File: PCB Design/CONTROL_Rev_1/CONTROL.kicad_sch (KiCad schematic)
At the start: 4 parts, among them J1 Conn_01x24_Pin, J2 Conn_01x24_Pin, U1 STM32F446RETx

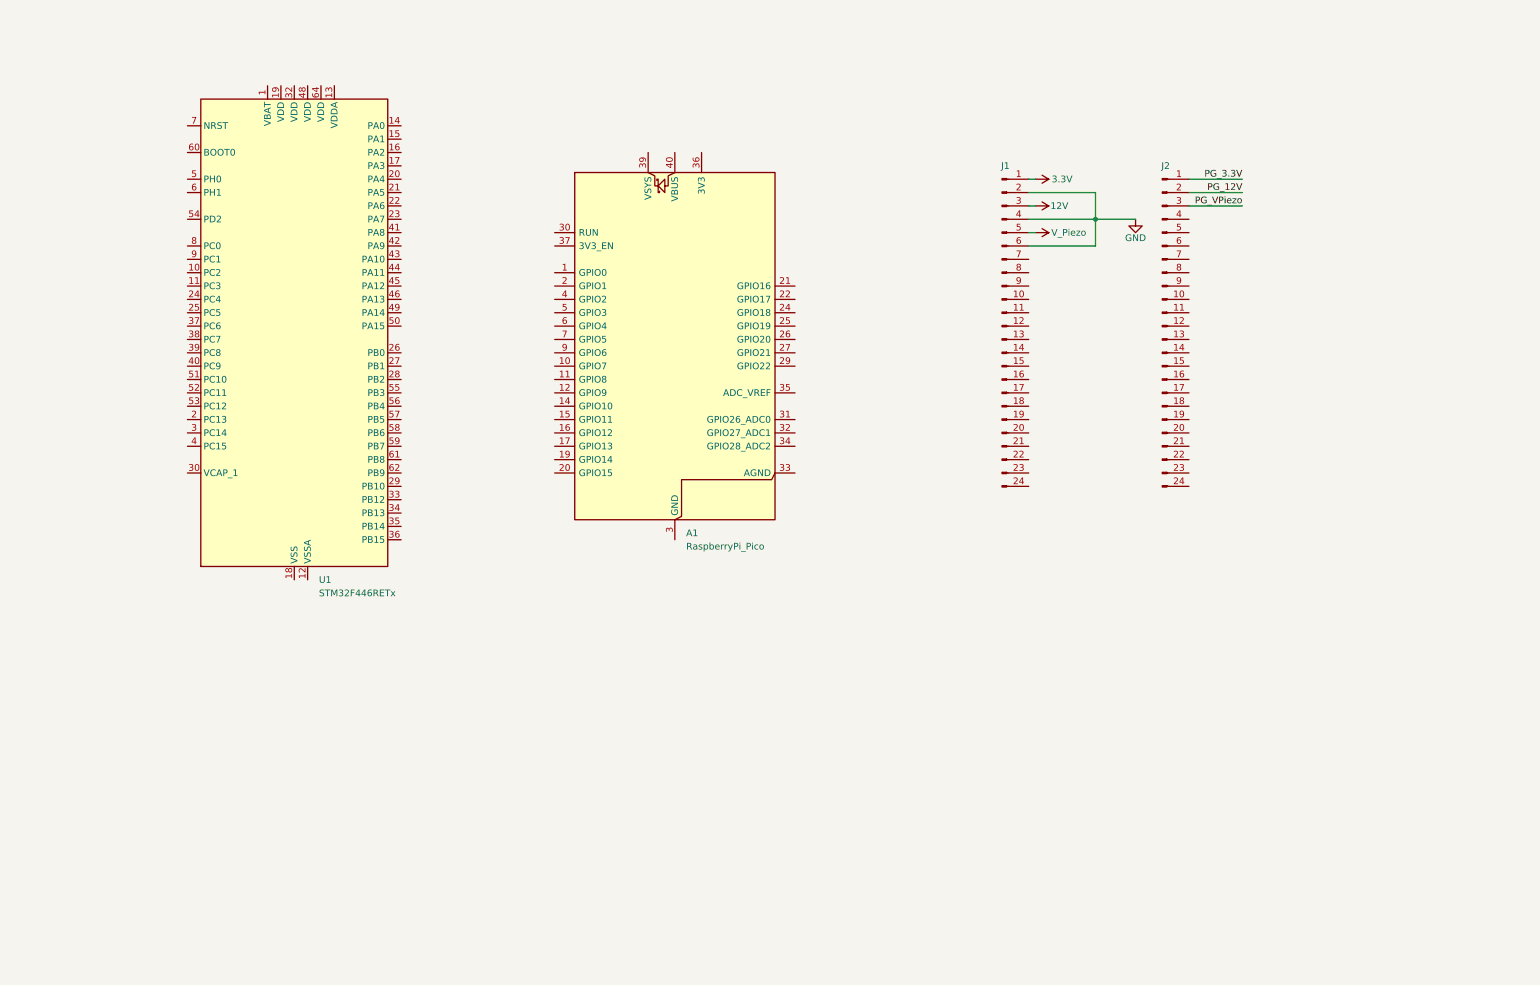
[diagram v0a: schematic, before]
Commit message: Initial Component Layout of Main MCU
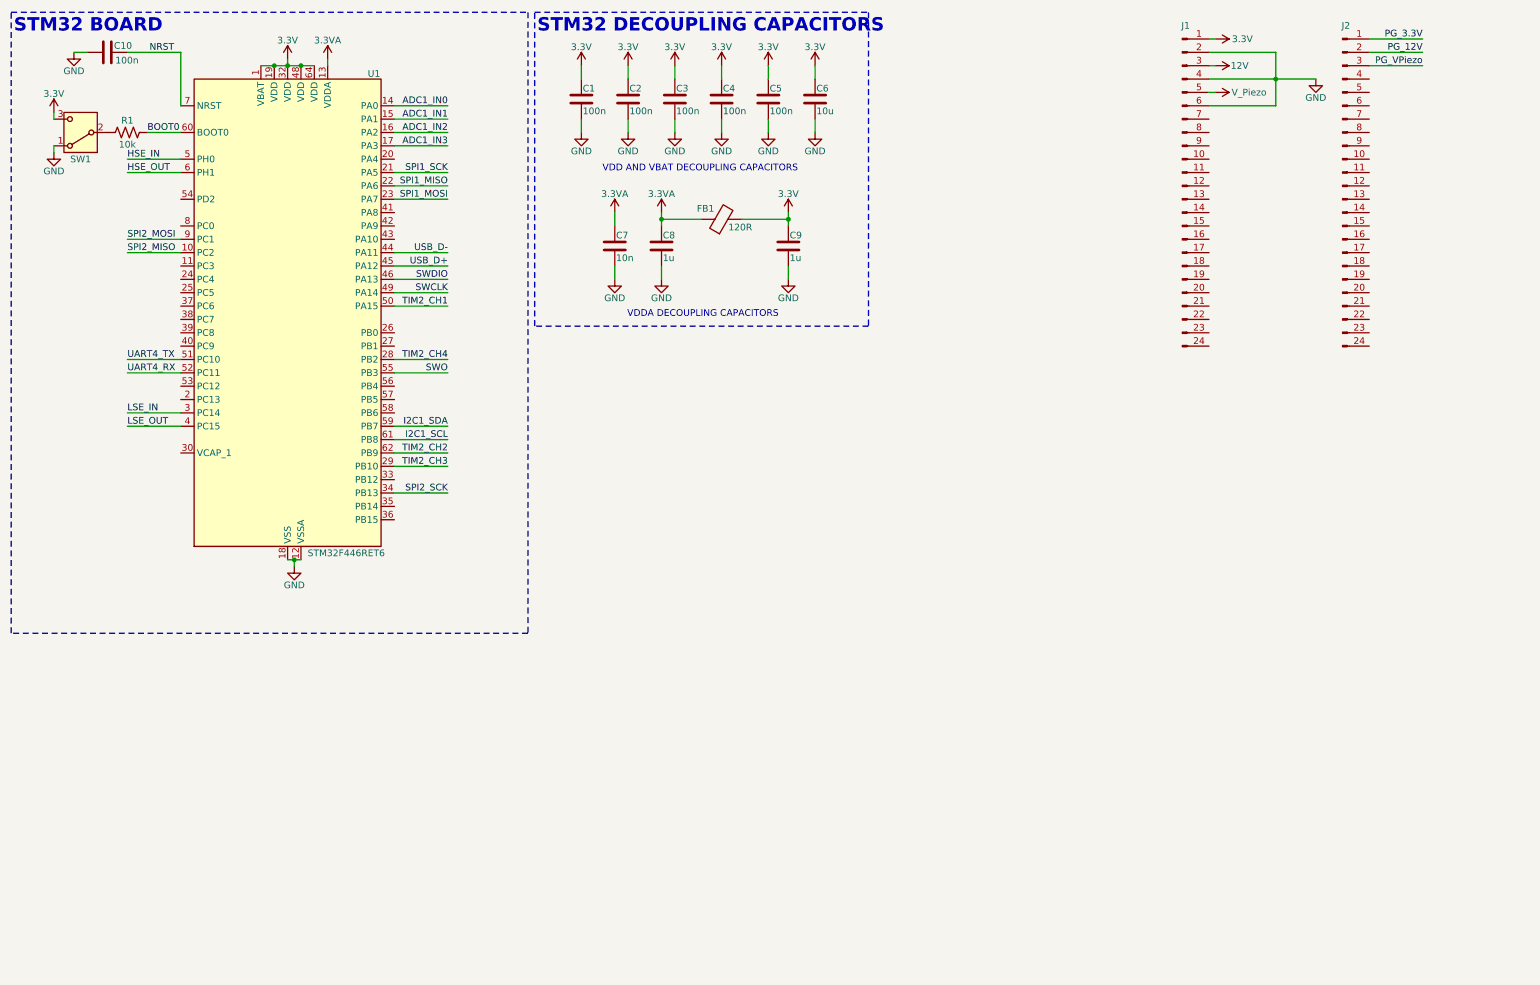
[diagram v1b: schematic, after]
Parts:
- removed A1: RaspberryPi_Pico, Module:RaspberryPi_Pico_Common_Unspecified, symbol MCU_Module:RaspberryPi_Pico
- added C1, C10, C2, C3, C4, C5: 100n, Capacitor_SMD:C_0603_1608Metric, symbol Device:C
- added C6: 10u, Capacitor_SMD:C_0603_1608Metric, symbol Device:C
- added C7: 10n, Capacitor_SMD:C_0603_1608Metric, symbol Device:C
- added C8, C9: 1u, Capacitor_SMD:C_0603_1608Metric, symbol Device:C
- added FB1: 120R, symbol Device:FerriteBead
- added R1: 10k, symbol Device:R_US
- added SW1: SW_SPDT, symbol Switch:SW_SPDT
- U1: value STM32F446RETx -> STM32F446RET6
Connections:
- net 3.3V: now also U1.1 (VBAT), U1.19 (VDD), U1.32 (VDD), U1.48 (VDD), U1.64 (VDD), C1.1, C2.1, C3.1, C4.1, C5.1, C6.1, C9.1, FB1.2, SW1.3 (C)
- net GND: now also U1.12 (VSSA), U1.18 (VSS), U1.31 (VSS), U1.47 (VSS), U1.63 (VSS), C1.2, C10.1, C2.2, C3.2, C4.2, C5.2, C6.2, C7.2, C8.2, C9.2, SW1.1 (A)
- net SPI2_MISO: now reaches U1.10 (PC2)
- net 3.3VA: now reaches U1.13 (VDDA)
- net 3.3VA: now also C7.1, C8.1, FB1.1
- net ADC1_IN0: now reaches U1.14 (PA0)
- net ADC1_IN1: now reaches U1.15 (PA1)
- net ADC1_IN2: now reaches U1.16 (PA2)
- net ADC1_IN3: now reaches U1.17 (PA3)
- net SPI1_SCK: now reaches U1.21 (PA5)
- net SPI1_MISO: now reaches U1.22 (PA6)
- net SPI1_MOSI: now reaches U1.23 (PA7)
- net TIM2_CH4: now reaches U1.28 (PB2)
- net TIM2_CH3: now reaches U1.29 (PB10)
- net LSE_IN: now reaches U1.3 (PC14)
- net SPI2_SCK: now reaches U1.34 (PB13)
- net LSE_OUT: now reaches U1.4 (PC15)
- net USB_D-: now reaches U1.44 (PA11)
- net USB_D+: now reaches U1.45 (PA12)
- net SWDIO: now reaches U1.46 (PA13)
- net SWCLK: now reaches U1.49 (PA14)
- net HSE_IN: now reaches U1.5 (PH0)
- net TIM2_CH1: now reaches U1.50 (PA15)
- net UART4_TX: now reaches U1.51 (PC10)
- net UART4_RX: now reaches U1.52 (PC11)
- net SWO: now reaches U1.55 (PB3)
- net I2C1_SDA: now reaches U1.59 (PB7)
- net HSE_OUT: now reaches U1.6 (PH1)
- net BOOT0: now reaches U1.60 (BOOT0)
- net BOOT0: now also R1.2
- net I2C1_SCL: now reaches U1.61 (PB8)
- net TIM2_CH2: now reaches U1.62 (PB9)
- net NRST: now reaches U1.7 (NRST)
- net NRST: now also C10.2
- net SPI2_MOSI: now reaches U1.9 (PC1)
- new net: R1.1, SW1.2 (B)
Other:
- note added: "STM32 BOARD"
- note added: "STM32 DECOUPLING CAPACITORS"
- note added: "VDD AND VBAT DECOUPLING CAPACITORS"
- note added: "VDDA DECOUPLING CAPACITORS"
- moved on the sheet: J1, J2, U1

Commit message: Finished Schematic, Started Placing Components on PCB
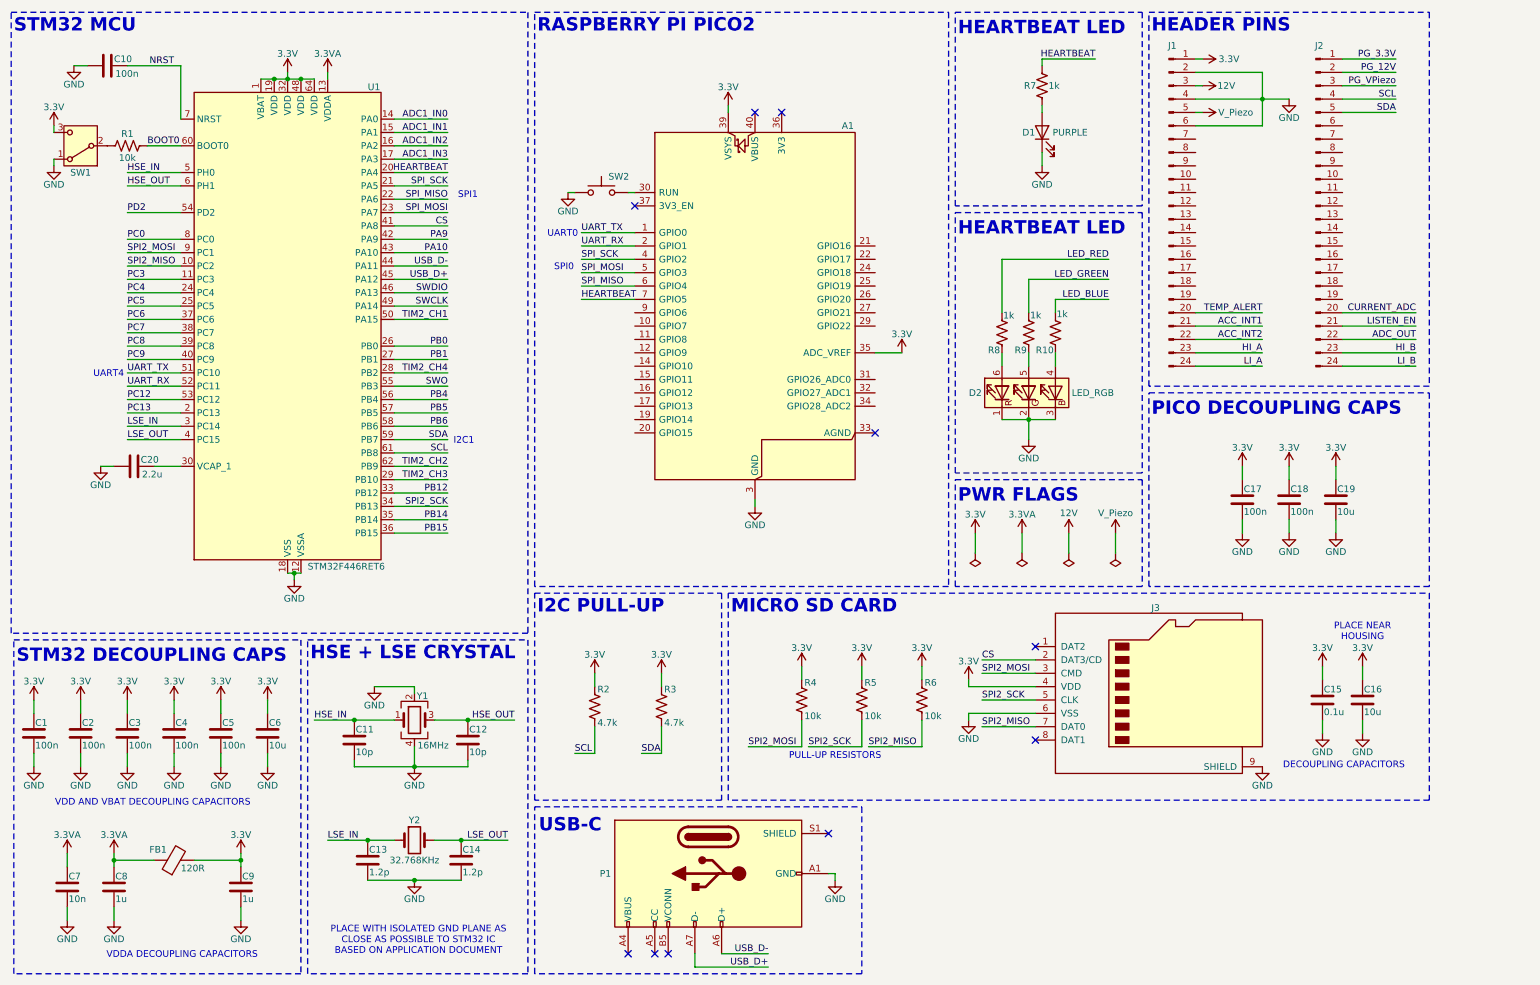
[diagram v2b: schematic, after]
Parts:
- added A1: RaspberryPi_Pico, Module:RaspberryPi_Pico_Common_Unspecified, symbol MCU_Module:RaspberryPi_Pico
- added C11, C12: 10p, Capacitor_SMD:C_0603_1608Metric, symbol Device:C
- added C13, C14: 1.2p, Capacitor_SMD:C_0603_1608Metric, symbol Device:C
- added C15: 0.1u, Capacitor_SMD:C_0603_1608Metric, symbol Device:C
- added C16, C19: 10u, Capacitor_SMD:C_0603_1608Metric, symbol Device:C
- added C17, C18: 100n, Capacitor_SMD:C_0603_1608Metric, symbol Device:C
- added C20: 2.2u, Capacitor_SMD:C_0603_1608Metric, symbol Device:C
- added D1: PURPLE, CONTROL:JB2835AWTWU57EA0000N0000001, symbol Device:LED
- added D2: LED_RGB, LED_SMD:LED_RGB_PLCC-6, symbol Device:LED_RGB
- added J3: Micro_SD_Card, CONTROL:AMPHENOL_1140084168, symbol Connector:Micro_SD_Card
- added P1: USB_C_Plug_USB2.0, CONTROL:AMPHENOL_10164359-00011LF, symbol Connector:USB_C_Plug_USB2.0
- added R10, R7, R8, R9: 1k, Resistor_SMD:R_0603_1608Metric, symbol Device:R_US
- added R2, R3: 4.7k, Resistor_SMD:R_0603_1608Metric, symbol Device:R_US
- added R4, R5, R6: 10k, Resistor_SMD:R_0603_1608Metric, symbol Device:R_US
- added SW2: SW_Push, Button_Switch_SMD:SW_Tactile_SPST_NO_Straight_CK_PTS636Sx25SMTRLFS, symbol Switch:SW_Push
- added Y1: 16MHz, symbol Device:Crystal_GND24
- added Y2: 32.768KHz, CONTROL:XTAL_ABS05W-32.768KHZ-D-2-T, symbol Device:Crystal
- FB1: footprint (none) -> Inductor_SMD:L_0201_0603Metric
- R1: footprint (none) -> Resistor_SMD:R_0603_1608Metric
- SW1: footprint (none) -> CONTROL:B-TYPE
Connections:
- net I2C1_SCL is gone; now on net SCL: U1.61 (PB8)
- net I2C1_SDA is gone; now on net SDA: U1.59 (PB7)
- net 3.3V: now also A1.35 (ADC_VREF), A1.39 (VSYS), C15.1, C16.1, C17.1, C18.1, C19.1, J3.4 (VDD), R2.1, R3.1, R4.1, R5.1, R6.1
- net GND: now also A1.13 (GND), A1.18 (GND), A1.23 (GND), A1.28 (GND), A1.3 (GND), A1.38 (GND), A1.8 (GND), C11.2, C12.2, C13.2, C14.2, C15.2, C16.2, C17.2, C18.2, C19.2, C20.1, D1.1 (K), D2.1 (RK), D2.2 (GK), D2.3 (BK), J3.6 (VSS), J3.9 (SHIELD), P1.A1 (GND), P1.A12 (GND), P1.B1 (GND), P1.B12 (GND), SW2.1, Y1.2, Y1.4
- net HSE_IN: now also C11.1, Y1.1
- net HSE_OUT: now also C12.1, Y1.3
- net LSE_IN: now also C13.1, Y2.1
- net LSE_OUT: now also C14.1, Y2.2
- net SPI2_MISO: now also J3.7 (DAT0), R6.2
- net SPI2_MOSI: now also J3.3 (CMD), R4.2
- net SPI2_SCK: now also J3.5 (CLK), R5.2
- net USB_D+: now also P1.A7 (D-)
- net USB_D-: now also P1.A6 (D+)
- net CURRENT_ADC: now reaches J2.20 (Pin_20)
- net LISTEN_EN: now reaches J2.21 (Pin_21)
- net ADC_OUT: now reaches J2.22 (Pin_22)
- net HI_B: now reaches J2.23 (Pin_23)
- net LI_B: now reaches J2.24 (Pin_24)
- net SCL: now reaches J2.4 (Pin_4)
- net SCL: now also R2.2
- net SDA: now reaches J2.5 (Pin_5)
- net SDA: now also R3.2
- net TEMP_ALERT: now reaches J1.20 (Pin_20)
- net ACC_INT1: now reaches J1.21 (Pin_21)
- net ACC_INT2: now reaches J1.22 (Pin_22)
- net HI_A: now reaches J1.23 (Pin_23)
- net LI_A: now reaches J1.24 (Pin_24)
- net PC3: now reaches U1.11 (PC3)
- net PC13: now reaches U1.2 (PC13)
- net HEARTBEAT: now reaches U1.20 (PA4)
- net HEARTBEAT: now also A1.7 (GPIO5), R7.2
- net PC4: now reaches U1.24 (PC4)
- net PC5: now reaches U1.25 (PC5)
- net PB0: now reaches U1.26 (PB0)
- net PB1: now reaches U1.27 (PB1)
- net at U1.30 (VCAP_1): now also C20.2
- net PB12: now reaches U1.33 (PB12)
- net PB14: now reaches U1.35 (PB14)
- net PB15: now reaches U1.36 (PB15)
- net PC6: now reaches U1.37 (PC6)
- net PC7: now reaches U1.38 (PC7)
- net PC8: now reaches U1.39 (PC8)
- net PC9: now reaches U1.40 (PC9)
- net CS: now reaches U1.41 (PA8)
- net CS: now also J3.2 (DAT3/CD)
- net PA9: now reaches U1.42 (PA9)
- net PA10: now reaches U1.43 (PA10)
- net PC12: now reaches U1.53 (PC12)
- net PD2: now reaches U1.54 (PD2)
- net PB4: now reaches U1.56 (PB4)
- net PB5: now reaches U1.57 (PB5)
- net PB6: now reaches U1.58 (PB6)
- net PC0: now reaches U1.8 (PC0)
- net SPI1_MISO renamed SPI_MISO
- net SPI_MISO: now also A1.6 (GPIO4)
- net SPI1_MOSI renamed SPI_MOSI
- net SPI_MOSI: now also A1.5 (GPIO3)
- net SPI1_SCK renamed SPI_SCK
- net SPI_SCK: now also A1.4 (GPIO2)
- net UART4_RX renamed UART_RX
- net UART_RX: now also A1.2 (GPIO1)
- net UART4_TX renamed UART_TX
- net UART_TX: now also A1.1 (GPIO0)
- new net: D1.2 (A), R7.1
- new net: D2.6 (RA), R8.1
- new net: D2.4 (BA), R10.1
- new net: D2.5 (GA), R9.1
- new net: A1.30 (RUN), SW2.2
- new net: P1.A4 (VBUS), P1.A9 (VBUS), P1.B4 (VBUS), P1.B9 (VBUS)
- new net LED_BLUE: R10.2
- new net LED_GREEN: R9.2
- new net LED_RED: R8.2
- no-connect marks 0 -> 10
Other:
- note added: "DECOUPLING CAPACITORS"
- note added: "HEADER PINS"
- note added: "HEARTBEAT LED"
- note added: "HSE + LSE CRYSTAL"
- note added: "I2C PULL-UP"
- note added: "I2C1"
- note added: "MICRO SD CARD"
- note added: "PICO DECOUPLING CAPS"
- note added: "PLACE NEAR HOUSING"
- note added: "PLACE WITH ISOLATED GND PLANE AS CLOSE AS POSSIBLE TO STM32 IC BASED ON APPLICATION DOCUMENT"
- note added: "PULL-UP RESISTORS"
- note added: "PWR FLAGS"
- note added: "RASPBERRY PI PICO2"
- note added: "SPI0"
- note added: "SPI1"
- note added: "STM32 DECOUPLING CAPS"
- note added: "STM32 MCU"
- note added: "UART0"
- note added: "UART4"
- note added: "USB-C"
- note removed: "STM32 BOARD"
- note removed: "STM32 DECOUPLING CAPACITORS"
- company: (none) -> CAPSTONE
- title: (none) -> SWARM CONTROL BOARD
- moved on the sheet: C1, C10, C2, C3, C4, C5, C6, C7, C8, C9, FB1, J1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

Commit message: Minor Schematic Updates and PCB Routing
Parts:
- removed SW2: SW_Push, Button_Switch_SMD:SW_Tactile_SPST_NO_Straight_CK_PTS636Sx25SMTRLFS, symbol Switch:SW_Push
- A1: footprint Module:RaspberryPi_Pico_Common_Unspecified -> Module:RaspberryPi_Pico_Common_THT
- P1: footprint CONTROL:AMPHENOL_10164359-00011LF -> Connector_USB:USB_C_Receptacle_GCT_USB4085
- Y1: footprint (none) -> Crystal:Crystal_SMD_3225-4Pin_3.2x2.5mm
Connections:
- net ACC_INT1 is gone; now on net PB0: J1.21 (Pin_21)
- net ACC_INT2 is gone; now on net PB1: J1.22 (Pin_22)
- net PB4 is gone; now on net LED_BLUE: U1.56 (PB4)
- net PB5 is gone; now on net LISTEN_EN: U1.57 (PB5)
- net PC12 is gone; now on net LED_RED: U1.53 (PC12)
- net PD2 is gone; now on net LED_GREEN: U1.54 (PD2)
- net PG_12V is gone; now on net PC0: J2.2 (Pin_2)
- net PG_3.3V is gone; now on net PC3: J2.1 (Pin_1)
- net PG_VPiezo is gone; now on net PC13: J2.3 (Pin_3)
- net TEMP_ALERT is gone; now on net PC5: J1.20 (Pin_20)
- net TIM2_CH1 is gone; now on net LI_B: U1.50 (PA15)
- net TIM2_CH2 is gone; now on net HI_B: U1.62 (PB9)
- net TIM2_CH3 is gone; now on net LI_A: U1.29 (PB10)
- net TIM2_CH4 is gone; now on net HI_A: U1.28 (PB2)
- net ADC1_IN0: now also J1.15 (Pin_15)
- net ADC1_IN1: now also J1.17 (Pin_17)
- net ADC1_IN2: now also J1.16 (Pin_16)
- net ADC1_IN3: now also J1.18 (Pin_18)
- net ADC_OUT: no longer J2.22 (Pin_22)
- net CURRENT_ADC: no longer J2.20 (Pin_20)
- net LISTEN_EN: now also J2.22 (Pin_22); no longer J2.21 (Pin_21)
- net PA10: now also J2.18 (Pin_18)
- net PA9: now also J2.17 (Pin_17)
- net PB6: now also J2.21 (Pin_21)
- net PC4: now also J1.19 (Pin_19)
- net PC8: now also J2.15 (Pin_15)
- net PC9: now also J2.16 (Pin_16)
- net SCL: now also J2.19 (Pin_19); no longer J2.4 (Pin_4)
- net SDA: now also J2.20 (Pin_20); no longer J2.5 (Pin_5)
- no-connect marks 10 -> 11
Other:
- note added: "FIX"

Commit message: Completed Rev1 and Documentation
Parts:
- removed P1: USB_C_Plug_USB2.0, Connector_USB:USB_C_Receptacle_GCT_USB4085, symbol Connector:USB_C_Plug_USB2.0
- added D3: MINT, CONTROL:JB2835AWTWU57EA0000N0000001, symbol Device:LED
- added J4: USB_C_Receptacle_USB2.0_16P, Connector_USB:USB_C_Receptacle_GCT_USB4085, symbol Connector:USB_C_Receptacle_USB2.0_16P
- added R11, R12: 5.1k, Resistor_SMD:R_0603_1608Metric, symbol Device:R_US
- added R13: 1k, Resistor_SMD:R_0603_1608Metric, symbol Device:R_US
- C13, C14: footprint Capacitor_SMD:C_0603_1608Metric -> Capacitor_SMD:C_0402_1005Metric
- FB1: footprint Inductor_SMD:L_0201_0603Metric -> Inductor_SMD:L_0603_1608Metric
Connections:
- net ADC1_IN0: now also J1.16 (Pin_16); no longer J1.15 (Pin_15)
- net ADC1_IN2: now also J1.18 (Pin_18); no longer J1.16 (Pin_16)
- net ADC1_IN3: now also J1.19 (Pin_19); no longer J1.18 (Pin_18)
- net BOOT0: now also A1.25 (GPIO19)
- net GND: now also D3.1 (K), J4.A1 (GND), J4.A12 (GND), J4.B1 (GND), J4.B12 (GND), J4.S1 (SHIELD), R11.2, R12.2
- net NRST: now also A1.24 (GPIO18)
- net PB12: now also J2.10 (Pin_10)
- net PB14: now also J2.11 (Pin_11)
- net PB15: now also J2.12 (Pin_12)
- net PC4: now also J2.9 (Pin_9); no longer J1.19 (Pin_19)
- net PC6: now also J2.13 (Pin_13)
- net PC7: now also J2.14 (Pin_14)
- net SWCLK: now also A1.27 (GPIO21)
- net SWDIO: now also A1.29 (GPIO22)
- net SWO: now also A1.26 (GPIO20)
- net USB_D+: now also J4.A6 (D+), J4.B6 (D+)
- net USB_D-: now also J4.A7 (D-), J4.B7 (D-)
- net GPIO_28: now reaches J2.4 (Pin_4)
- net GPIO_28: now also A1.34 (GPIO28_ADC2)
- net GPIO_27: now reaches J2.5 (Pin_5)
- net GPIO_27: now also A1.32 (GPIO27_ADC1)
- net GPIO_26: now reaches J2.6 (Pin_6)
- net GPIO_26: now also A1.31 (GPIO26_ADC0)
- net GPIO_17: now reaches J2.7 (Pin_7)
- net GPIO_17: now also A1.22 (GPIO17)
- net GPIO_16: now reaches J2.8 (Pin_8)
- net GPIO_16: now also A1.21 (GPIO16)
- net GPIO_7: now reaches A1.10 (GPIO7)
- net GPIO_7: now also J1.8 (Pin_8)
- net GPIO_8: now reaches A1.11 (GPIO8)
- net GPIO_8: now also J1.9 (Pin_9)
- net GPIO_9: now reaches A1.12 (GPIO9)
- net GPIO_9: now also J1.10 (Pin_10)
- net GPIO_10: now reaches A1.14 (GPIO10)
- net GPIO_10: now also J1.11 (Pin_11)
- net GPIO_11: now reaches A1.15 (GPIO11)
- net GPIO_11: now also J1.12 (Pin_12)
- net GPIO_12: now reaches A1.16 (GPIO12)
- net GPIO_12: now also J1.13 (Pin_13)
- net GPIO_13: now reaches A1.17 (GPIO13)
- net GPIO_13: now also J1.14 (Pin_14)
- net GPIO_14: now reaches A1.19 (GPIO14)
- net GPIO_14: now also J1.15 (Pin_15)
- net GPIO_15: now reaches A1.20 (GPIO15)
- net GPIO_15: now also R13.2
- net GPIO_6: now reaches A1.9 (GPIO6)
- net GPIO_6: now also J1.7 (Pin_7)
- net LISTEN_EN renamed PB5
- new net: J4.A5 (CC1), R11.1
- new net: D3.2 (A), R13.1
- new net: J4.B5 (CC2), R12.1
- new net: J4.A4 (VBUS), J4.A9 (VBUS), J4.B4 (VBUS), J4.B9 (VBUS)
- no-connect marks 11 -> 10
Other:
- note removed: "FIX"
- moved on the sheet: D1, R7
